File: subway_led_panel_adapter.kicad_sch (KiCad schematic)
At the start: 28 parts, among them J1 Conn_02x06_Odd_Even, J2 Conn_02x10_Odd_Even, J3 Conn_02x06_Odd_Even, J4 Conn_02x20_Odd_Even, U1 74AHCT244, U2 ChinaBluePill, U3 74LVC1G123

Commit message: more work
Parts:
- added H1, H2: MountingHole_Pad, MountingHole:MountingHole_3.2mm_M3_Pad, symbol Mechanical:MountingHole_Pad
- added R9: 1k, Resistor_SMD:R_0603_1608Metric, symbol Device:R
- R3: value 1k -> 100k
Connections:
- net GND: now also H1.1, H2.1, R9.1
- net LE/MOD/CA_LV: now also R9.2
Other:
- note added: "100kOhm, 100nF at 5V time constant: 10ms"
- note added: "Break out all the GPIOs!"
- note added: "Make sure that LED panel row drivers (via E2) only are enabled when LE pin is regularly going L->H (then we assume the controller is alive)"
- note added: "first LED panel in chain 'controller' port"
- note added: "last LED panel in chain output port"
- moved on the sheet: C1, C2, C3, D1, D2, D3, D4, J1, J2, J3, J4, JP1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

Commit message: general cleanup
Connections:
- net GND: no longer J1.10 (Pin_10), J3.10 (Pin_10)
- net PA10: now also J3.10 (Pin_10)
- net PA15: now also J1.10 (Pin_10)
- no-connect marks 24 -> 27
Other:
- note added: "LE"
- note added: "MCU hung..."
- note added: "ROW_E2"
- note added: "ROW_E2 high for a brief period after latching signal LEx has regular L→H transisions. Tries to avoid burning out the LEDs displaying a static row (when MCU gets hung, for example)."
- note added: "Regular refresh..."
- note added: "USB"
- note added: "XTAL LED"
- note added: "approx 10ms"
- note added: "first panel controller port"
- note added: "last panel output"
- note added: "⇐ panel column driver chain A ⇐"
- note added: "⇐ panel column driver chain B ⇐"
- note added: "⇐ panel column driver chain C ⇐"
- note removed: "Make sure that LED panel row drivers (via E2) only are enabled when LE pin is regularly going L->H (then we assume the controller is alive)"
- moved on the sheet: C2, C3, D1, D2, D3, D4, H1, H2, J1, J3, JP1, JP2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

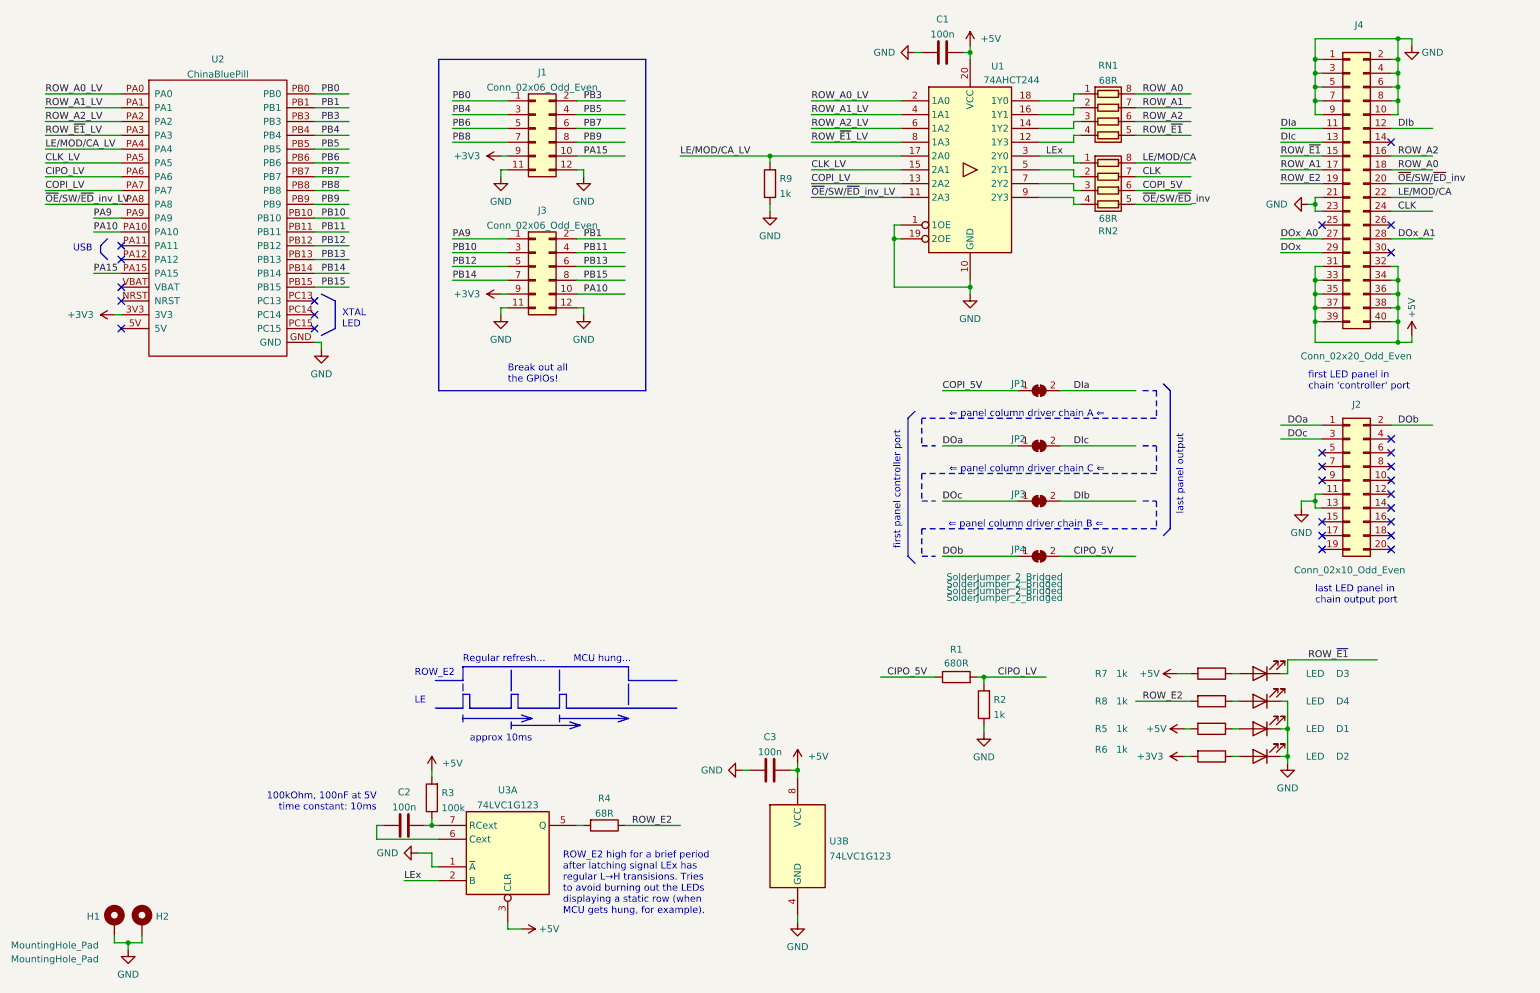
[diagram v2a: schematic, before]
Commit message: Add "pmpd" style connector for 3v3 signals, rearrange, add mounting holes.
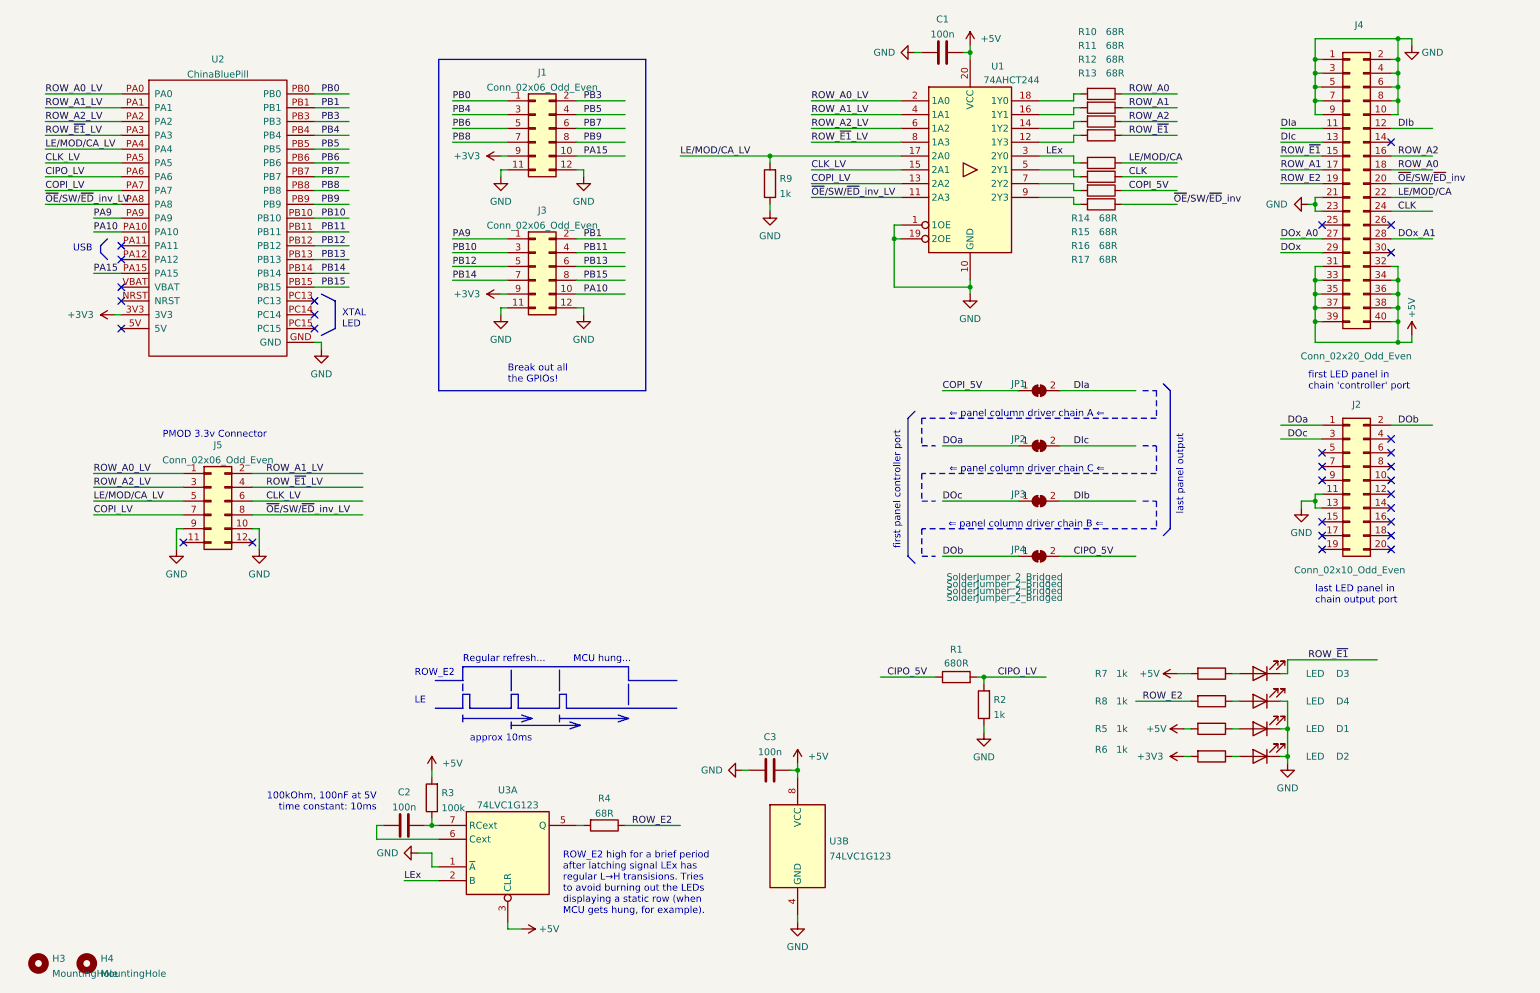
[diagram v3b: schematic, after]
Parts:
- removed H1, H2: MountingHole_Pad, MountingHole:MountingHole_3.2mm_M3_Pad, symbol Mechanical:MountingHole_Pad
- removed RN1, RN2: 68R, Resistor_SMD:R_Array_Concave_4x0402, symbol Device:R_Pack04
- added H3, H4: MountingHole, MountingHole:MountingHole_4.3mm_M4, symbol Mechanical:MountingHole
- added J5: Conn_02x06_Odd_Even, Connector_PinHeader_2.54mm:PinHeader_2x06_P2.54mm_Vertical, symbol Connector_Generic:Conn_02x06_Odd_Even
- added R10, R11, R12, R13, R14, R15, R16, R17: 68R, Resistor_SMD:R_0603_1608Metric, symbol Device:R
- J2: footprint Connector_IDC:IDC-Header_2x10_P2.54mm_Latch_Horizontal -> Connector_PinHeader_2.54mm:PinHeader_2x10_P2.54mm_Vertical
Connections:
- net CLK: now also R15.1
- net CLK_LV: now also J5.6 (Pin_6)
- net COPI_5V: now also R16.1
- net COPI_LV: now also J5.7 (Pin_7)
- net GND: now also J5.10 (Pin_10), J5.9 (Pin_9)
- net LEx: now also R14.2
- net LE/MOD/CA: now also R14.1
- net LE/MOD/CA_LV: now also J5.5 (Pin_5)
- net ROW_A0: now also R10.1
- net ROW_A0_LV: now also J5.1 (Pin_1)
- net ROW_A1: now also R11.1
- net ROW_A1_LV: now also J5.2 (Pin_2)
- net ROW_A2: now also R12.1
- net ROW_A2_LV: now also J5.3 (Pin_3)
- net ROW_~{E1}: now also R13.1
- net ROW_~{E1}_LV: now also J5.4 (Pin_4)
- net ~{OE}/SW/~{ED}_inv: now also R17.1
- net ~{OE}/SW/~{ED}_inv_LV: now also J5.8 (Pin_8)
- net at U1.18 (1Y0): now also R10.2
- net at U1.16 (1Y1): now also R11.2
- net at U1.14 (1Y2): now also R12.2
- net at U1.12 (1Y3): now also R13.2
- net at U1.5 (2Y1): now also R15.2
- net at U1.7 (2Y2): now also R16.2
- net at U1.9 (2Y3): now also R17.2
- no-connect marks 27 -> 29
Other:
- note added: "PMOD 3.3v Connector"

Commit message: further work
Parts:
- added C4: 100n, Capacitor_SMD:C_0603_1608Metric, symbol Device:C
- added D5, D6, D7, D8: LED, LED_SMD:LED_0603_1608Metric, symbol Device:LED
- added JP5, JP6: SolderJumper_2_Bridged, Jumper:SolderJumper-2_P1.3mm_Bridged_Pad1.0x1.5mm, symbol Jumper:SolderJumper_2_Bridged
- added R18, R19, R20, R21: 1k, Resistor_SMD:R_0603_1608Metric, symbol Device:R
- added R22: 68R, Resistor_SMD:R_0603_1608Metric, symbol Device:R
- added U4: 74LVC1GU04DRL, Package_TO_SOT_SMD:SOT-553, symbol 74xGxx:74LVC1GU04DRL
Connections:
- net +5V: now also R8.2, C4.2, JP6.2 (B), U4.5 (VCC); no longer J4.31 (Pin_31), J4.32 (Pin_32), J4.33 (Pin_33), J4.34 (Pin_34), J4.35 (Pin_35), J4.36 (Pin_36), J4.37 (Pin_37), J4.38 (Pin_38), J4.39 (Pin_39), J4.40 (Pin_40)
- net GND: now also C4.1, D5.1 (K), D6.1 (K), D7.1 (K), D8.1 (K), JP5.2 (B), U4.3 (GND); no longer D4.1 (K), J4.1 (Pin_1), J4.10 (Pin_10), J4.2 (Pin_2), J4.3 (Pin_3), J4.4 (Pin_4), J4.5 (Pin_5), J4.6 (Pin_6), J4.7 (Pin_7), J4.8 (Pin_8), J4.9 (Pin_9)
- net PB12: now also R21.2
- net PB13: now also R20.2
- net PB14: now also R19.2
- net PB15: now also R18.2
- net at R4.2, U3.5 (Q): now also U4.2
- net ROW_E2 renamed ROW_~{E2}
- net ROW_~{E2}: now also D4.1 (K), R22.1; no longer R8.2
- new net: D8.2 (A), R21.1
- new net: J4.1 (Pin_1), J4.10 (Pin_10), J4.2 (Pin_2), J4.3 (Pin_3), J4.4 (Pin_4), J4.5 (Pin_5), J4.6 (Pin_6), J4.7 (Pin_7), J4.8 (Pin_8), J4.9 (Pin_9), JP5.1 (A)
- new net: J4.31 (Pin_31), J4.32 (Pin_32), J4.33 (Pin_33), J4.34 (Pin_34), J4.35 (Pin_35), J4.36 (Pin_36), J4.37 (Pin_37), J4.38 (Pin_38), J4.39 (Pin_39), J4.40 (Pin_40), JP6.1 (A)
- new net: D6.2 (A), R19.1
- new net: R22.2, U4.4
- new net: D5.2 (A), R18.1
- new net: D7.2 (A), R20.1
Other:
- note added: "ROW_~{E2}"
- note added: "ROW_~{E2} high for a brief period after latching signal LEx has regular L→H transisions. Tries to avoid burning out the LEDs displaying a static row (when MCU gets hung, for example)."
- note added: "choose polarity"
- note removed: "ROW_E2"
- note removed: "ROW_E2 high for a brief period after latching signal LEx has regular L→H transisions. Tries to avoid burning out the LEDs displaying a static row (when MCU gets hung, for example)."
- note removed: "first LED panel in chain 'controller' port"
- moved on the sheet: C2, C3, R3, R4, U3A, U3B
